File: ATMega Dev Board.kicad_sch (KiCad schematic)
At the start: 45 parts, among them J1 Conn_01x09, J2 Conn_01x04, J3 Conn_01x09, J4 SPI header, J5 USB-C_31-M-12, Q1 S8050, Q2 2N7002, Q3 HL6042, Q4 HL6042, SW1 SW_SPST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

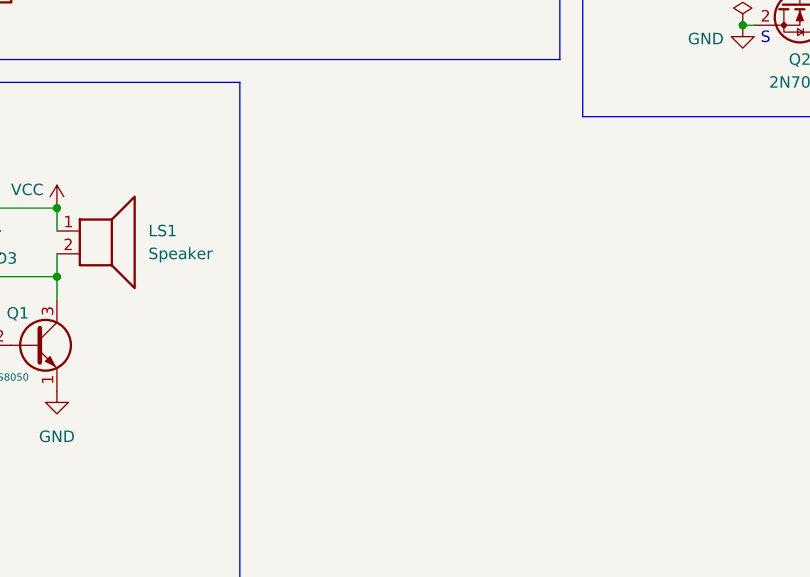
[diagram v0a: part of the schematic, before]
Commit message: added mounting holes
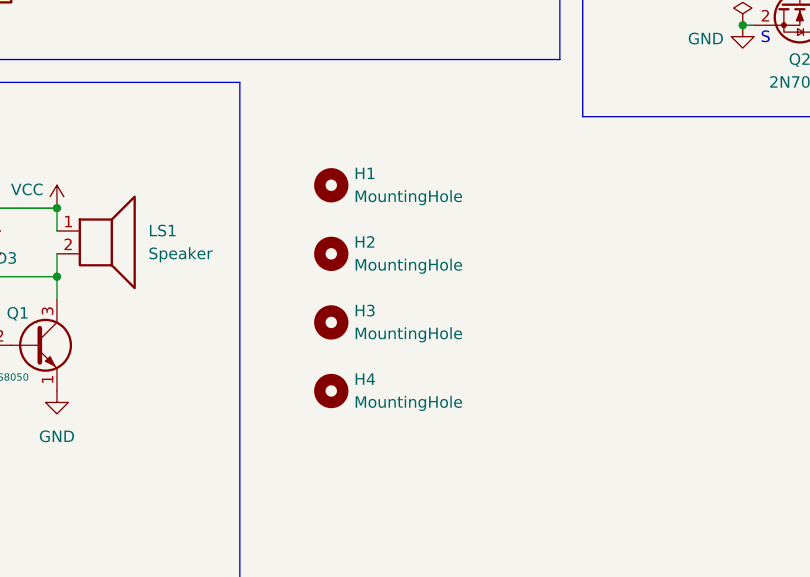
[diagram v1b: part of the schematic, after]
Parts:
- added H1, H2, H3, H4: MountingHole, MountingHole:MountingHole_2.2mm_M2_Pad_Via, symbol Mechanical:MountingHole

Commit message: better layout and new components
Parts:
- removed J2: Conn_01x04, Connector_PinSocket_2.54mm:PinSocket_1x04_P2.54mm_Vertical, symbol Connector_Generic:Conn_01x04
- F1: value 500mA/24V -> 1A; LCSC C70077 -> C69688
- H1, H2, H3, H4: footprint MountingHole:MountingHole_2.2mm_M2_Pad_Via -> MountingHole:MountingHole_2.1mm
- J1: value Conn_01x09 -> Conn_01x13; footprint Connector_PinSocket_2.54mm:PinSocket_1x09_P2.54mm_Vertical -> Connector_PinSocket_2.54mm:PinSocket_1x13_P2.54mm_Vertical; symbol Connector_Generic:Conn_01x09 -> Connector_Generic:Conn_01x13
- renumbered J3 to J2
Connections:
- net PA4: now also J1.10 (Pin_10)
- net PA5: now also J1.11 (Pin_11)
- net PA6: now also J1.12 (Pin_12)
- net PA7: now also J1.13 (Pin_13)
